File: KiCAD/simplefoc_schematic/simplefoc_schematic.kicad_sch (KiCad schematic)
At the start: 59 parts, among them J1 Power Supply, J2 Motor Connector, J3 Sensor Connector, J4 Conn_02x03_Odd_Even, J5 Programming Port, J6 UART Port, J7 Conn_01x03, Q1 IRF740, Q2 IRF740, Q3 IRF740, Q4 IRF740, Q5 IRF740, Q6 IRF740, SW1 SW_Push, U1 IR2130, U2 STM32F101CBT6, U3 LM317L_SOT-89, U4 TS 1117, Y1 8MHz

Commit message: Added a standalone schematic for the STM32 part Moved from ir2130 driver to the TMC6140
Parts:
- removed C1: 47uF, Capacitor_SMD:CP_Elec_3x5.3, symbol Device:C_Polarized
- removed C14, C15, C16, C17, C21, C22, C23: 2.2uF, Capacitor_SMD:C_0805_2012Metric, symbol Device:C
- removed C19: 100nF, Capacitor_SMD:C_0805_2012Metric, symbol Device:C
- removed C2, C3: 10uF, Capacitor_SMD:CP_Elec_3x5.3, symbol Device:C_Polarized
- removed C20: 4.7uF, Capacitor_SMD:C_0805_2012Metric, symbol Device:C
- removed C5: 470nF, symbol Device:C
- removed C6, C7, C8: 220uF/63V, Capacitor_SMD:CP_Elec_5x3, symbol Device:C_Polarized
- removed D1, D2, D3: D, symbol Device:D
- removed J4: Conn_02x03_Odd_Even, symbol Connector_Generic:Conn_02x03_Odd_Even
- removed R10, R9: 10k, Resistor_SMD:R_0805_2012Metric, symbol Device:R
- removed R12, R8: 1k, Resistor_SMD:R_0805_2012Metric, symbol Device:R
- removed R13, R14: ?, Resistor_SMD:R_0805_2012Metric, symbol Device:R
- removed R2: 4.7R, Resistor_SMD:R_0805_2012Metric, symbol Device:R
- removed R7: 0.05R/5W, Resistor_SMD:R_0805_2012Metric, symbol Device:R
- removed U1: IR2130, SO-28W, symbol IR2130:IR2130
- removed U3: LM317L_SOT-89, Package_TO_SOT_SMD:SOT-89-3, symbol Regulator_Linear:LM317L_SOT-89
- removed U4: TS 1117, Package_TO_SOT_SMD:SOT-223, symbol Regulator_Linear:L7806
- added C1, C2: 100nF, Capacitor_SMD:C_0603_1608Metric, symbol Device:C_Small
- added C14: 10uF, Capacitor_SMD:C_0603_1608Metric, symbol Device:C_Polarized_Small
- added C15, C17, C20, C22, C23, C24, C27: 100nF/35V, Capacitor_SMD:C_0603_1608Metric, symbol Device:C_Small
- added C16, C19, C21: 10uF/35V, Capacitor_SMD:C_0603_1608Metric, symbol Device:C_Small
- added C25, C26: 20uF/6.3V, Capacitor_SMD:C_0603_1608Metric, symbol Device:C_Small
- added C3: 10nF, Capacitor_SMD:C_0603_1608Metric, symbol Device:C_Small
- added C5: 1uF, Capacitor_SMD:C_0603_1608Metric, symbol Device:C_Polarized_Small
- added C6, C7: 470nF/16V, Capacitor_SMD:C_0603_1608Metric, symbol Device:C_Small
- added C8: 1nF/50V, Capacitor_SMD:C_0603_1608Metric, symbol Device:C_Small
- added D1, D2: D_Schottky, Diode_SMD:D_SMA, symbol Device:D_Schottky
- added IC1: TMC6140-Trinamic, Package_DFN_QFN:QFN-36-1EP_5x6mm_P0.5mm_EP3.6x4.1mm, symbol tmc6140-trinamic:TMC6140-Trinamic
- added L1: 33uH, symbol Device:L_Small
- added R10, R8, R9: 1mOhm/3W, Resistor_SMD:R_2512_6332Metric, symbol Device:R_Small
- added R2: 4.7k, Resistor_SMD:R_0603_1608Metric, symbol Device:R_Small
- added R7: FBead, Resistor_SMD:R_0805_2012Metric, symbol Device:R_Small
- C10, C11: value 270nF -> 1nF/50V; footprint (none) -> Capacitor_SMD:C_0603_1608Metric
- C13, C18, C4: footprint Capacitor_SMD:C_0805_2012Metric -> Capacitor_SMD:C_0603_1608Metric
- C9: value 270nF -> 470nF/16V; footprint (none) -> Capacitor_SMD:C_0603_1608Metric
- Q1, Q2, Q3, Q4, Q5, Q6: value IRF740 -> IRLR 2905; footprint Package_TO_SOT_THT:TO-220-3_Vertical -> Package_TO_SOT_SMD:TO-252-2
- R1, R3, R4, R5, R6: value 4.7R -> 2.2R; footprint Resistor_SMD:R_0805_2012Metric -> Resistor_SMD:R_0603_1608Metric
- R11: value 100k -> 2.2R; footprint Resistor_SMD:R_0805_2012Metric -> Resistor_SMD:R_0603_1608Metric
- SW1: footprint (none) -> Additional_Components:SW_Push_SPST_Wuerth_434121043816
- Y1: footprint (none) -> Crystal:Crystal_SMD_HC49-SD
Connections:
- net SA is gone; now on net ENCA: J3.4 (Pin_4)
- net SB is gone; now on net ENCB: J3.3 (Pin_3)
- net SC is gone; now on net ENCC: J3.2 (Pin_2)
- net +3.3V: now also C1.1, C2.1, C25.2, C26.2, IC1.21 (VccIO), L1.1, R7.1; no longer U2.9 (VDDA)
- net +BATT: now also C15.2, C16.2, C17.2, C19.2, C20.2, C21.2, C23.2, D1.2 (A), IC1.11 (VS)
- net GND: now also C10.2, C11.2, U2.44 (BOOT0), C1.2, C14.2, C15.1, C16.1, C17.1, C19.1, C2.2, C20.1, C21.1, C23.1, C24.1, C25.1, C26.1, C27.1, C3.2, C5.2, C8.2, IC1.24 (~{SI}), IC1.37 (EP_GND), R10.2, R2.2, R8.2, R9.2
- net U: now also Q4.2 (D), C6.2, C8.1, IC1.7 (U_(BMU)); no longer C9.2, Q6.2 (D)
- net V: now also C10.1, Q1.3 (S), C7.2, IC1.4 (V_(BMV)); no longer C10.2, Q2.3 (S)
- net W: now also C11.1, C9.2, Q2.3 (S), Q6.2 (D), IC1.36 (W_(BMW)); no longer C11.2, Q1.3 (S), Q4.2 (D)
- net at R4.2: now also Q2.1 (G); no longer Q6.1 (G)
- net at R6.2: now also Q5.1 (G); no longer Q4.1 (G)
- net at R11.2: now also Q6.1 (G)
- net at R5.2: now also Q4.1 (G); no longer Q5.1 (G)
- net HO1: now reaches U2.11 (PA1)
- net HO1: now also IC1.13 (UH)
- net LO1: now reaches U2.12 (PA2)
- net LO1: now also IC1.14 (UL)
- net HO2: now reaches U2.13 (PA3)
- net HO2: now also IC1.15 (VH)
- net LO2: now reaches U2.14 (PA4)
- net LO2: now also IC1.16 (VL)
- net HO3: now reaches U2.15 (PA5)
- net HO3: now also IC1.17 (WH)
- net LO3: now reaches U2.16 (PA6)
- net LO3: now also IC1.18 (WL)
- net ENCA: now reaches U2.25 (PB12)
- net ENCB: now reaches U2.26 (PB13)
- net ENCC: now reaches U2.27 (PB14)
- net at C9.1: now also IC1.34 (BSW)
- net BOOT0 renamed LOUTW
- net LOUTW: now also IC1.1 (LSW); no longer U2.44 (BOOT0)
- net HOUT1 renamed HOUTU
- net HOUTU: now also IC1.8 (HSU)
- net HOUT3 renamed HOUTV
- net HOUTV: now also IC1.3 (HSV)
- net LOUT1 renamed HOUTW
- net HOUTW: now also IC1.35 (HSW)
- net LOUT2 renamed LOUTU
- net LOUTU: now also IC1.6 (LSU)
- net LOUT3 renamed LOUTV
- net LOUTV: now also IC1.5 (LSV)
- net OSCIN: no longer names the net of C13.2, U2.5 (PD0), Y1.2
- net OSCOUT: no longer names the net of C18.2, U2.6 (PD1), Y1.1
- net RESET: no longer names the net of C4.1, SW1.2, U2.7 (NRST)
- removed net VS0: Q4.3 (S), Q5.3 (S), Q6.3 (S)
- new net: C3.1, C5.1, R7.2, U2.9 (VDDA)
- new net: C14.1, IC1.33 (V10)
- new net: C6.1, IC1.9 (BSU)
- new net: C27.2, IC1.12 (VDD5)
- new net: C24.2, D2.1 (K), IC1.32 (VCP)
- new net: C7.1, IC1.2 (BSV)
- new net: C22.1, D1.1 (K), D2.2 (A)
- new net: C22.2, IC1.10 (SW), L1.2
- new net CURRU: IC1.22 (SO1)
- new net CURRV: IC1.23 (SO2)
- new net CURRW: IC1.25 (SO3)
- new net DIAG: IC1.20 (DIAG)
- new net DRV_STRENGTH: IC1.29 (DRV_STRENGTH)
- new net ENABLE: IC1.31 (ENABLE), R2.1
- new net GAIN: IC1.30 (LOW_GAIN)
- new net SensU: IC1.26 (SI1), Q4.3 (S), R9.1
- new net SensV: IC1.27 (SI2), Q5.3 (S), R8.1
- new net SensW: IC1.28 (SI3), Q6.3 (S), R10.1
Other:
- note added: "Place near VDD pins"
- note added: "Place near VDDA pin"
- note added: "TODO: - Footprint for inductor - Circuitry around SH_SET (see Documentation) - Calculate min Current for V_IO / is STM32 current sufficient? - Decide on connectors - Matching Pins on STM32 for analog in and DIAG (UART) in"
- note removed: "High power resistor"
- note removed: "Place near VDD"
- moved on the sheet: C13, C18, C4, J2, J3, Q3, R1, U2, Y1

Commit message: Finalized schematic and component selection for acquisition from distributor
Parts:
- added C28, C29, C30, C31: 1000uF/25V, Capacitor_SMD:CP_Elec_10x14.3, symbol Device:C_Polarized_Small
- added C32: 100nF/35V, Capacitor_SMD:C_0603_1608Metric, symbol Device:C_Small
- added C33: 10uF/6.3V, Capacitor_SMD:C_0603_1608Metric, symbol Device:C_Small
- added D3: D_Schottky, Diode_SMD:D_SMA, symbol Device:D_Schottky
- added R12, R13, R14: 47k, Resistor_SMD:R_0603_1608Metric, symbol Device:R_Small
- C1, C2, C4: value 100nF -> 100nF/6V
- C12: value 100nF -> 100nF/35V; footprint Capacitor_SMD:C_0805_2012Metric -> Capacitor_SMD:C_0603_1608Metric
- C13, C18: value 20pF -> 20pF/6V
- C14: value 10uF -> 10uF/35V; footprint Capacitor_SMD:C_0603_1608Metric -> Capacitor_SMD:CP_Elec_4x5.8
- C16, C19, C21: footprint Capacitor_SMD:C_0603_1608Metric -> Capacitor_SMD:CP_Elec_4x5.8; symbol Device:C_Small -> Device:C_Polarized_Small
- C25, C26: value 20uF/6.3V -> 10uF/6.3V
- C3: value 10nF -> 10nF/6V
- C5: value 1uF -> 1uF/6V
- J1: footprint TerminalBlock:TerminalBlock_Altech_AK300-2_P5.00mm -> TerminalBlock_Phoenix:TerminalBlock_Phoenix_MKDS-1,5-2_1x02_P5.00mm_Horizontal
- J2: footprint TerminalBlock:TerminalBlock_Altech_AK300-3_P5.00mm -> TerminalBlock_Phoenix:TerminalBlock_Phoenix_MKDS-1,5-3_1x03_P5.00mm_Horizontal
- J3: footprint Connector_JST:JST_XH_B6B-XH-A_1x06_P2.50mm_Vertical -> Connector_JST:JST_ZH_B6B-ZR_1x06_P1.50mm_Vertical
- L1: value 33uH -> 33uH/0.42A; footprint (none) -> Additional_Components:L_Fastron_1212_FPS
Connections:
- net +3.3V: now also C33.2
- net +BATT: now also C28.1, C29.1, C30.1, C31.1
- net CURRU: now also U2.18 (PB0)
- net CURRV: now also U2.19 (PB1)
- net CURRW: now also U2.17 (PA7)
- net GND: now also C28.2, C29.2, C30.2, C31.2, C32.1, C33.1, D3.2 (A), R14.1
- net at C22.2, IC1.10 (SW), L1.2: now also D3.1 (K)
- net at IC1.19 (SH_SET): now also C32.2, R12.2, R13.2, R14.2
- new net BRAKE-0: R12.1
- new net BRAKE-1: R13.1
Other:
- note added: "I_{Load}min = 9 mA"
- note added: "TODO: - Matching Pins on STM32 for DIAG (UART) in"
- note removed: "TODO: - Footprint for inductor - Circuitry around SH_SET (see Documentation) - Calculate min Current for V_IO / is STM32 current sufficient? - Decide on connectors - Matching Pins on STM32 for analog in and DIAG (UART) in"
- moved on the sheet: C27, R2

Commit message: Removed unused components and replaced some components with smaller ones
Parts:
- removed C12: 100nF/35V, Capacitor_SMD:C_0603_1608Metric, symbol Device:C
- removed C13, C18: 20pF/6V, Capacitor_SMD:C_0603_1608Metric, symbol Device:C
- removed C14, C16, C19, C21: 10uF/35V, Capacitor_SMD:CP_Elec_4x5.8, symbol Device:C_Polarized_Small
- removed C32: 100nF/35V, Capacitor_SMD:C_0603_1608Metric, symbol Device:C_Small
- removed C33: 10uF/6.3V, Capacitor_SMD:C_0603_1608Metric, symbol Device:C_Small
- removed D3: D_Schottky, Diode_SMD:D_SMA, symbol Device:D_Schottky
- removed R13: 47k, Resistor_SMD:R_0603_1608Metric, symbol Device:R_Small
- removed Y1: 8MHz, Crystal:Crystal_SMD_HC49-SD, symbol Device:Crystal
- added C12, C13, C14, C16, C19: 10uF/35V, Capacitor_SMD:C_0603_1608Metric, symbol Device:C_Small
- added C18: 100nF/35V, Capacitor_SMD:C_0603_1608Metric, symbol Device:C_Small
- added U1: MC7805CDTG, Package_TO_SOT_SMD:TO-252-2, symbol Regulator_Linear:MC78M05_TO252
- C25, C26: value 10uF/6.3V -> 22uF/6.3V
- D1, D2: footprint Diode_SMD:D_SMA -> Additional_Components:DIODE_MSS1P4-M3_89A
- J7: value Conn_01x03 -> Servo
- R10: value 1mOhm/3W -> 0R; footprint Resistor_SMD:R_2512_6332Metric -> Resistor_SMD:R_0603_1608Metric
- R12: value 47k -> 22k
- R7: value FBead -> 10k; footprint Resistor_SMD:R_0805_2012Metric -> Resistor_SMD:R_0603_1608Metric
- R8, R9: value 1mOhm/3W -> 10k; footprint Resistor_SMD:R_2512_6332Metric -> Resistor_SMD:R_0603_1608Metric
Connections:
- net BRAKE-0 is gone; now on an unnamed net: R12.1
- net +3.3V: now also C3.1, C5.1, J3.6 (Pin_6), R12.2, R8.1, R9.1, U2.9 (VDDA)
- net +5V: now also C19.1, U1.3 (VO); no longer J3.6 (Pin_6)
- net +BATT: now also C13.1, C14.1, C16.1, C18.2, U1.1 (VI)
- net DIAG: now also U2.13 (PA3)
- net ENABLE: now also U2.15 (PA5)
- net ENCA: now also R7.2, U2.19 (PB1); no longer U2.25 (PB12)
- net ENCB: now also R8.2, U2.18 (PB0); no longer U2.26 (PB13)
- net ENCC: now also R9.2, U2.17 (PA7); no longer U2.27 (PB14)
- net GND: now also IC1.26 (SI1), IC1.27 (SI2), IC1.28 (SI3), Q4.3 (S), Q5.3 (S), Q6.3 (S), C12.1, C13.2, C14.2, C16.2, C18.1, C19.2, U1.2 (GND); no longer R10.2, R8.2, R9.2
- net HO1: now also U2.29 (PA8); no longer U2.11 (PA1)
- net HO2: now also U2.30 (PA9); no longer U2.13 (PA3)
- net HO3: now also U2.31 (PA10); no longer U2.15 (PA5)
- net LO1: now also U2.26 (PB13); no longer U2.12 (PA2)
- net LO2: now also U2.27 (PB14); no longer U2.14 (PA4)
- net LO3: now also U2.28 (PB15); no longer U2.16 (PA6)
- net RX: now also U2.43 (PB7)
- net Servo: now also U2.10 (PA0)
- net TX: now also U2.42 (PB6)
- net at IC1.33 (V10): now also C12.2
- net at IC1.19 (SH_SET), R14.2: no longer R12.2
- net at IC1.10 (SW), L1.2: now also R10.1; no longer C22.2
- net CURRU: no longer names the net of IC1.22 (SO1)
- net CURRU: no longer U2.18 (PB0)
- net CURRV: no longer names the net of IC1.23 (SO2)
- net CURRV: no longer U2.19 (PB1)
- net CURRW: no longer names the net of IC1.25 (SO3)
- net CURRW: no longer U2.17 (PA7)
- net DRV_STRENGTH: no longer names the net of IC1.29 (DRV_STRENGTH)
- net GAIN: no longer names the net of IC1.30 (LOW_GAIN)
- removed net SensU: IC1.26 (SI1), Q4.3 (S), R9.1
- removed net SensV: IC1.27 (SI2), Q5.3 (S), R8.1
- removed net SensW: IC1.28 (SI3), Q6.3 (S), R10.1
- net Thermo: no longer names the net of J3.5 (Pin_5)
- new net: C22.2, R10.2
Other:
- note added: "Only close when VS < 15V"
- note added: "TODO: - Matching Pins on STM32 for DIAG (UART) in - Testpads for relevant pins"
- note removed: "TODO: - Matching Pins on STM32 for DIAG (UART) in"
- moved on the sheet: C17, C20, C28, C29, C3, C30, C31, C4, C5, J3, J5, J6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

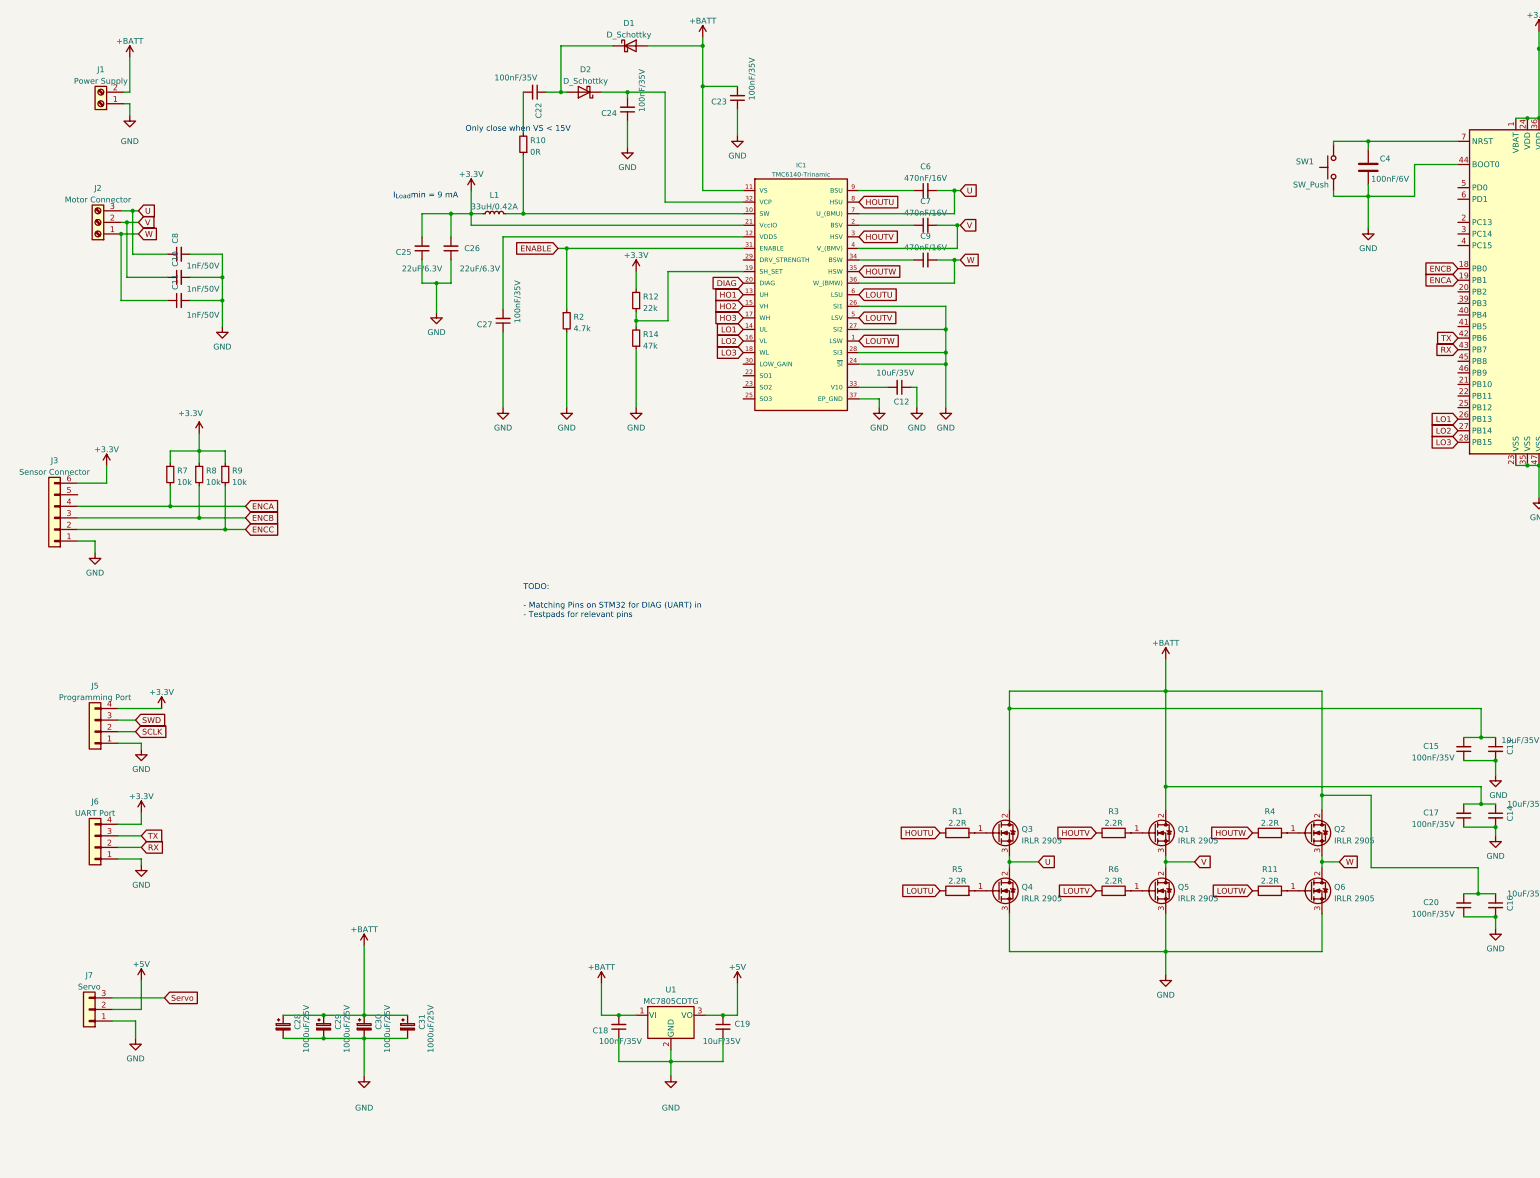
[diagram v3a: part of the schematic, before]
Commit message: Created first board layout for test board
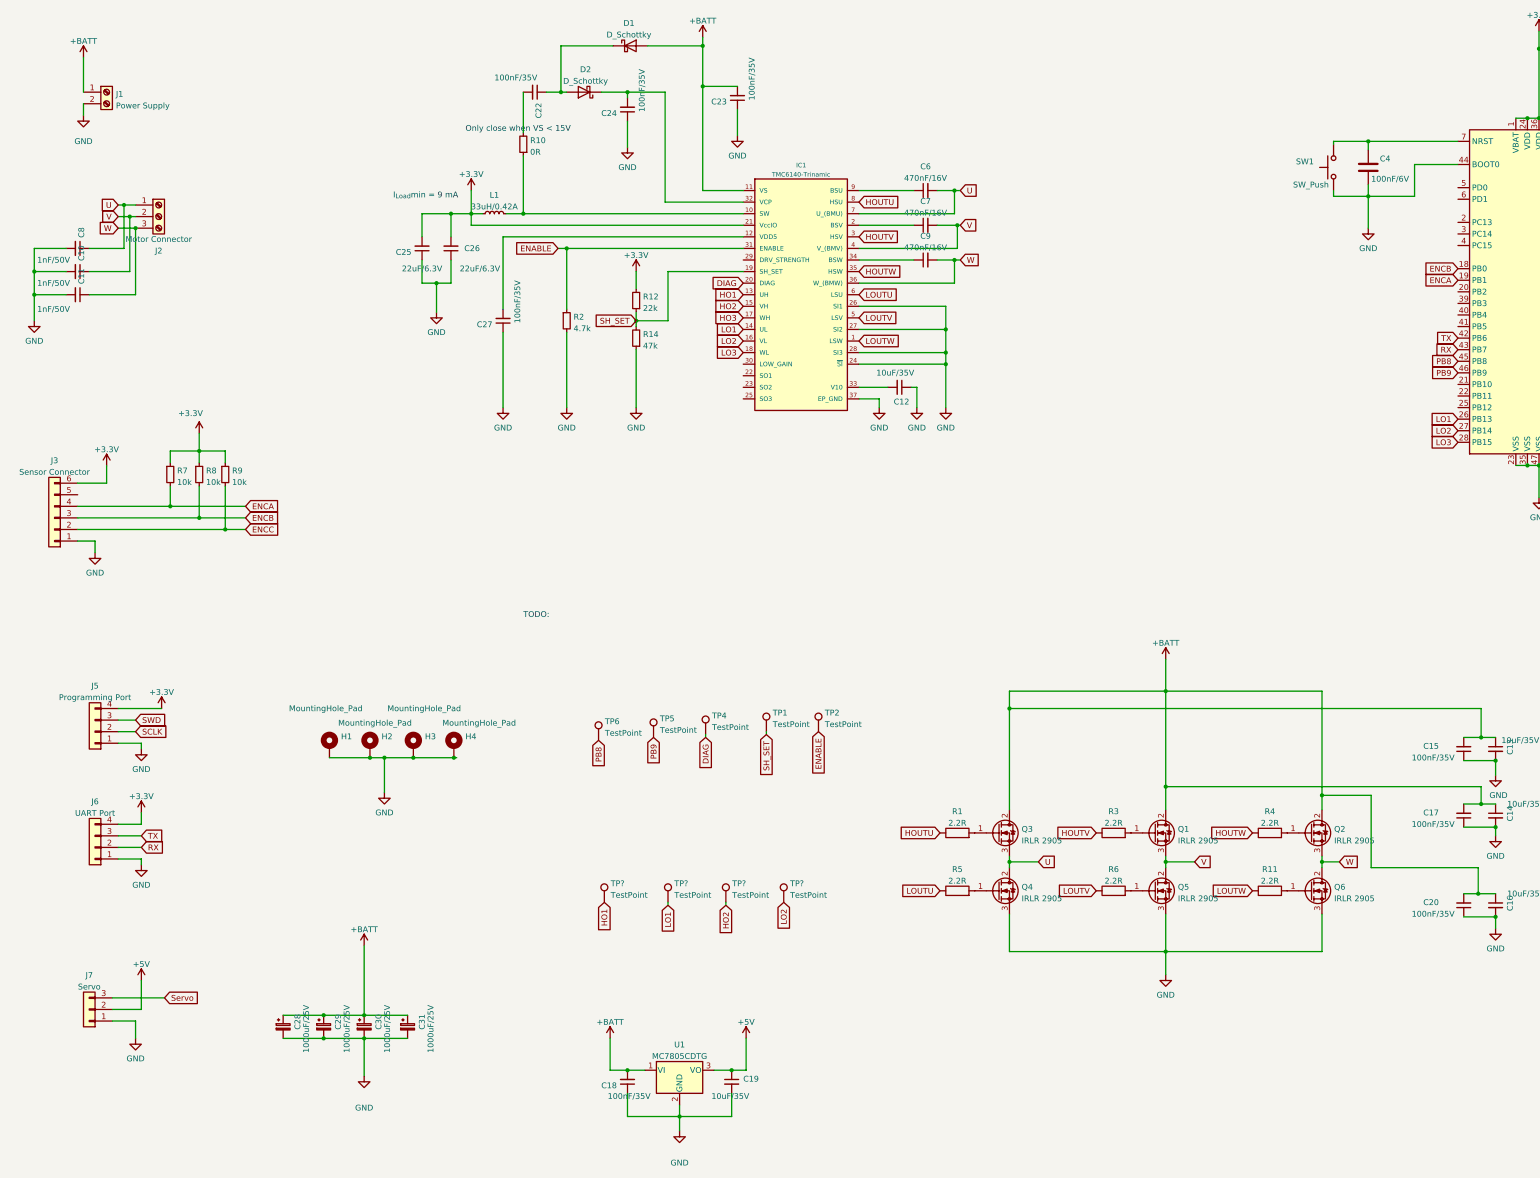
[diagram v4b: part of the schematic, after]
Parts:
- added H1, H2, H3, H4: MountingHole_Pad, MountingHole:MountingHole_2.5mm_Pad, symbol Mechanical:MountingHole_Pad
- added TP1, TP2, TP4, TP5, TP6: TestPoint, TestPoint:TestPoint_Pad_1.5x1.5mm, symbol Connector:TestPoint
- added TP? (x4): TestPoint, TestPoint:TestPoint_Pad_D1.0mm, symbol Connector:TestPoint
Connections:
- net +BATT: now also J1.1 (Pin_1); no longer J1.2 (Pin_2)
- net DIAG: now also TP4.1
- net ENABLE: now also TP2.1
- net GND: now also J1.2 (Pin_2), H1.1, H2.1, H3.1, H4.1; no longer J1.1 (Pin_1)
- net HO1: now also TP?.1
- net HO2: now also TP?.1
- net LO1: now also TP?.1
- net LO2: now also TP?.1
- net U: now also J2.1 (Pin_1); no longer J2.3 (Pin_3)
- net W: now also J2.3 (Pin_3); no longer J2.1 (Pin_1)
- net SH_SET: now reaches IC1.19 (SH_SET), R12.1, R14.2
- net SH_SET: now also TP1.1
- net PB8: now reaches U2.45 (PB8)
- net PB8: now also TP6.1
- net PB9: now reaches U2.46 (PB9)
- net PB9: now also TP5.1
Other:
- note added: "TODO:"
- note removed: "TODO: - Matching Pins on STM32 for DIAG (UART) in - Testpads for relevant pins"
- moved on the sheet: C10, C11, C18, C19, C8, J1, J2, U1
